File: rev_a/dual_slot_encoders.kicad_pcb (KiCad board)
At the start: 2 copper layers, 15 parts, among them U1 GP1S094HCZ0F, U2 GP1S094HCZ0F, U3 GPS1S97HCZ0F, U4 GPS1S97HCZ0F

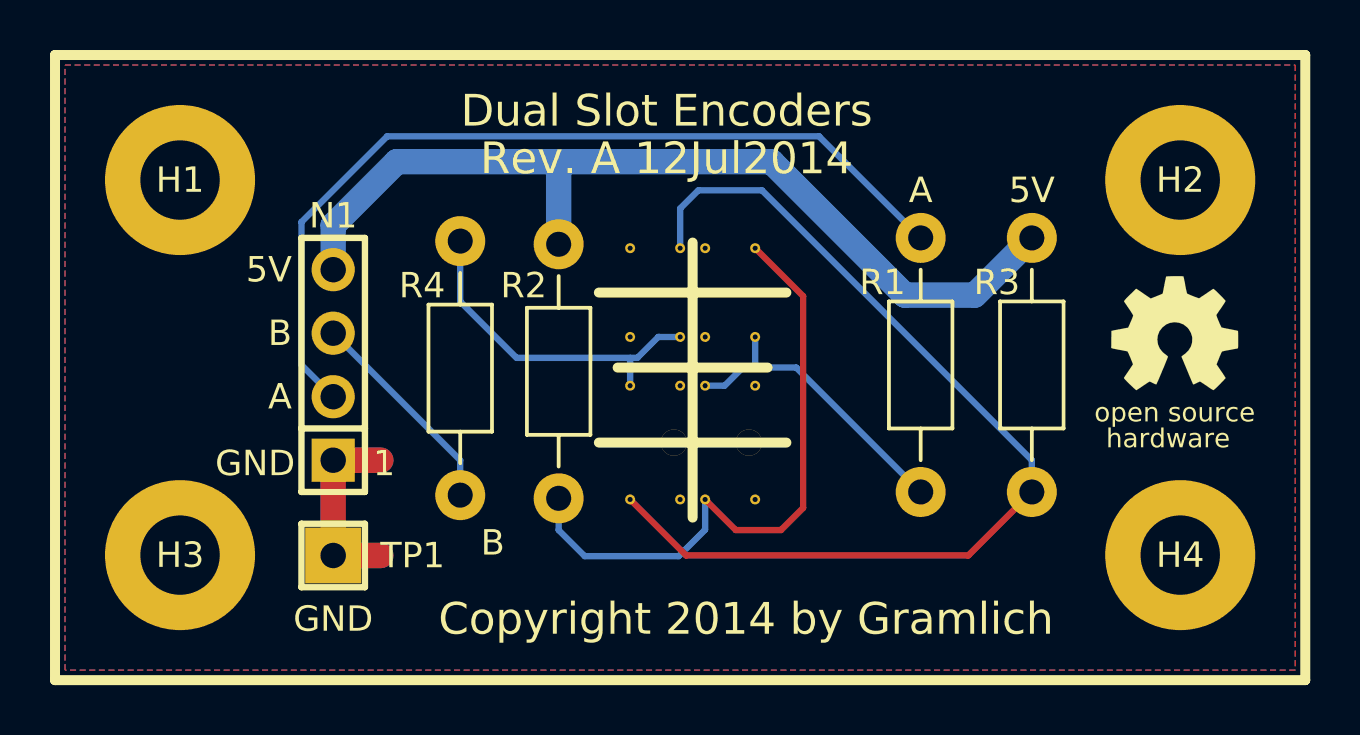
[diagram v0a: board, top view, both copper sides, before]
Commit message: Added edge cuts.
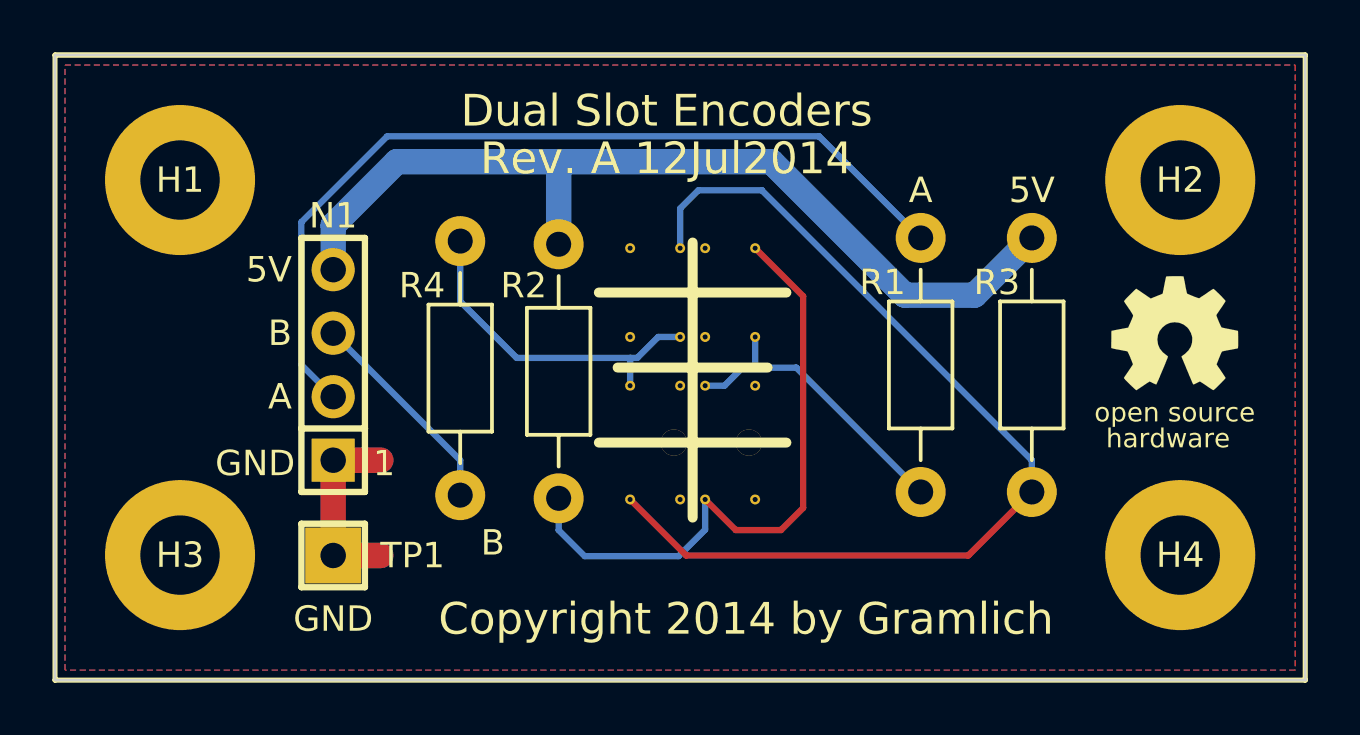
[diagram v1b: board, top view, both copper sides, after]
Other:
- board outline added: 50 x 25 mm
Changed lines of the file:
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@@
     (links 25)
     (no_connects 0)
-    (area 99.799999 99.799999 150.200001 125.3568)
+    (area 99.898399 99.898399 150.101601 125.3568)
     (thickness 1.6)
-    (drawings 27)
+    (drawings 31)
     (tracks 54)
     (zones 0)
@@
     (zone_45_only no)
     (trace_min 0.254)
-    (segment_width 0.4)
+    (segment_width 0.2032)
     (edge_width 0.1)
     (via_size 0.889)
@@
     (visible_elements 7FFEFFFF)
     (pcbplotparams
-      (layerselection 15761409)
+      (layerselection 284196865)
       (usegerberextensions true)
       (excludeedgelayer true)
@@
     )
   )
+  (gr_line (start 100 125) (end 100 100) (angle 90) (layer Edge.Cuts) (width 0.1))
+  (gr_line (start 150 125) (end 100 125) (angle 90) (layer Edge.Cuts) (width 0.1))
+  (gr_line (start 150 100) (end 150 125) (angle 90) (layer Edge.Cuts) (width 0.1))
+  (gr_line (start 100 100) (end 150 100) (angle 90) (layer Edge.Cuts) (width 0.1))
   (gr_text GND (at 111.125 122.555) (layer F.SilkS)
     (effects (font (size 1.016 1.016) (thickness 0.2032)))
@@
   (gr_line (start 125.5 107.5) (end 125.5 118.5) (angle 90) (layer F.SilkS) (width 0.4))
   (gr_line (start 122.5 112.5) (end 128.5 112.5) (angle 90) (layer F.SilkS) (width 0.4))
-  (gr_line (start 100 125) (end 100 100) (angle 90) (layer F.SilkS) (width 0.4))
-  (gr_line (start 150 125) (end 100 125) (angle 90) (layer F.SilkS) (width 0.4))
-  (gr_line (start 150 100) (end 150 125) (angle 90) (layer F.SilkS) (width 0.4))
-  (gr_line (start 100 100) (end 150 100) (angle 90) (layer F.SilkS) (width 0.4))
+  (gr_line (start 100 125) (end 100 100) (angle 90) (layer F.SilkS) (width 0.2032))
+  (gr_line (start 150 125) (end 100 125) (angle 90) (layer F.SilkS) (width 0.2032))
+  (gr_line (start 150 100) (end 150 125) (angle 90) (layer F.SilkS) (width 0.2032))
+  (gr_line (start 100 100) (end 150 100) (angle 90) (layer F.SilkS) (width 0.2032))
   (gr_line (start 100 100) (end 150 100) (angle 90) (layer F.SilkS) (width 0.2))
   (segment (start 128 112.5) (end 129.645 112.5) (width 0.254) (layer B.Cu) (net 1))
